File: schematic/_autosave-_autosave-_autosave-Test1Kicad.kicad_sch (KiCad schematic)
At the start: 49 parts, among them IC1 BMI055, J1 Power Module 1, J2 Power Module 2, J3 USB, J4 Telemetry 1, J5 Telemetry 2, J6 UART & I2C B, J7 CAN 1, J8 CAN 2, J9 GPS Module, U1 STM32F765IIKx, U10 TJA1051TK-3, U11 LT3080xDD, U2 NEO-M8N, U3 IST8310, U4 ICM-20602, U5 ICM-20689, U6 MS5611-01BA, U7 LT3080xDD, U8 STM32F103V8Tx, U9 TJA1051TK-3, Y1 ABM2-8.000MHZ-D4Y-T

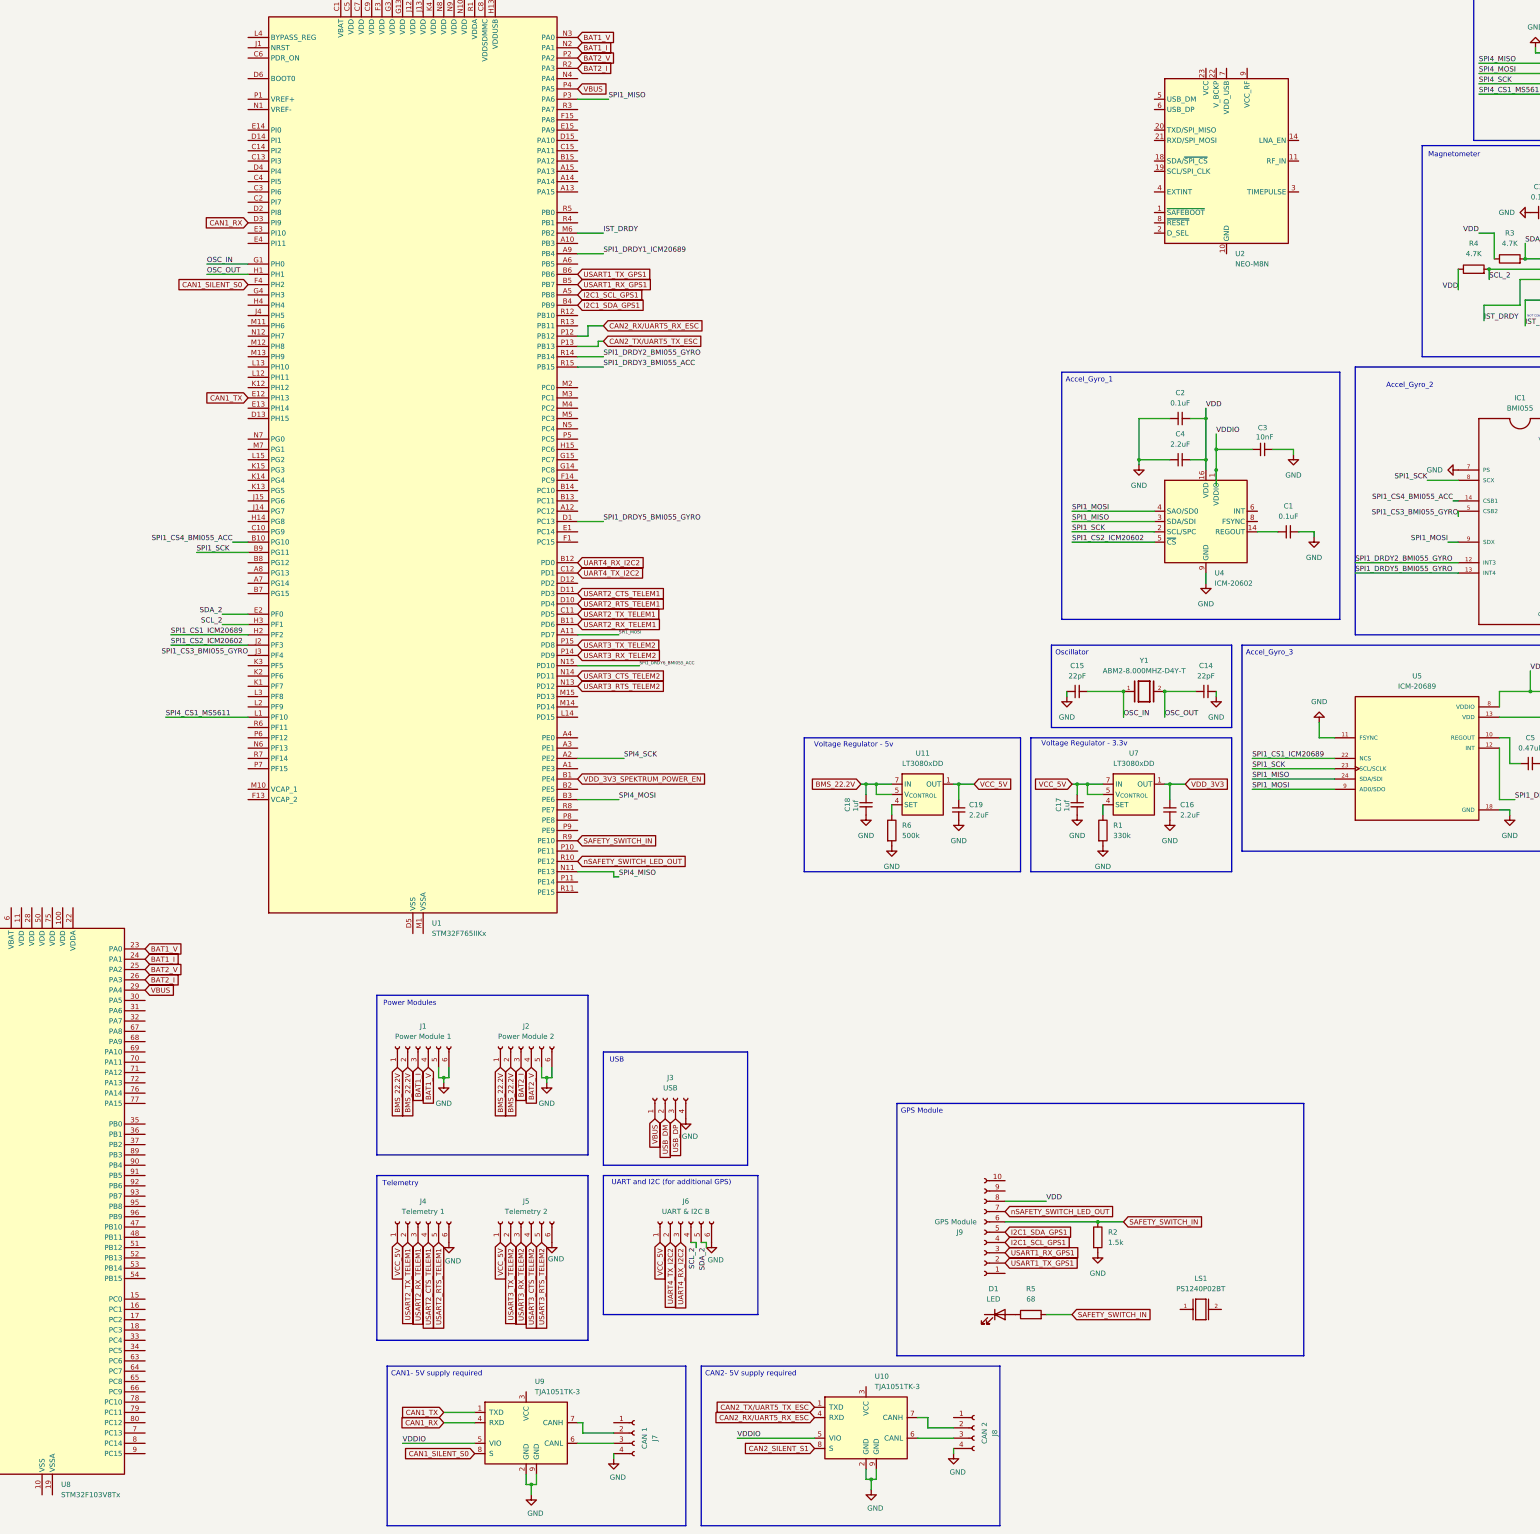
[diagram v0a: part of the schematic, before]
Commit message: CAP&ADC IN and SPI ports
also renamed UART&I2CB's SDA and SCL wire labels
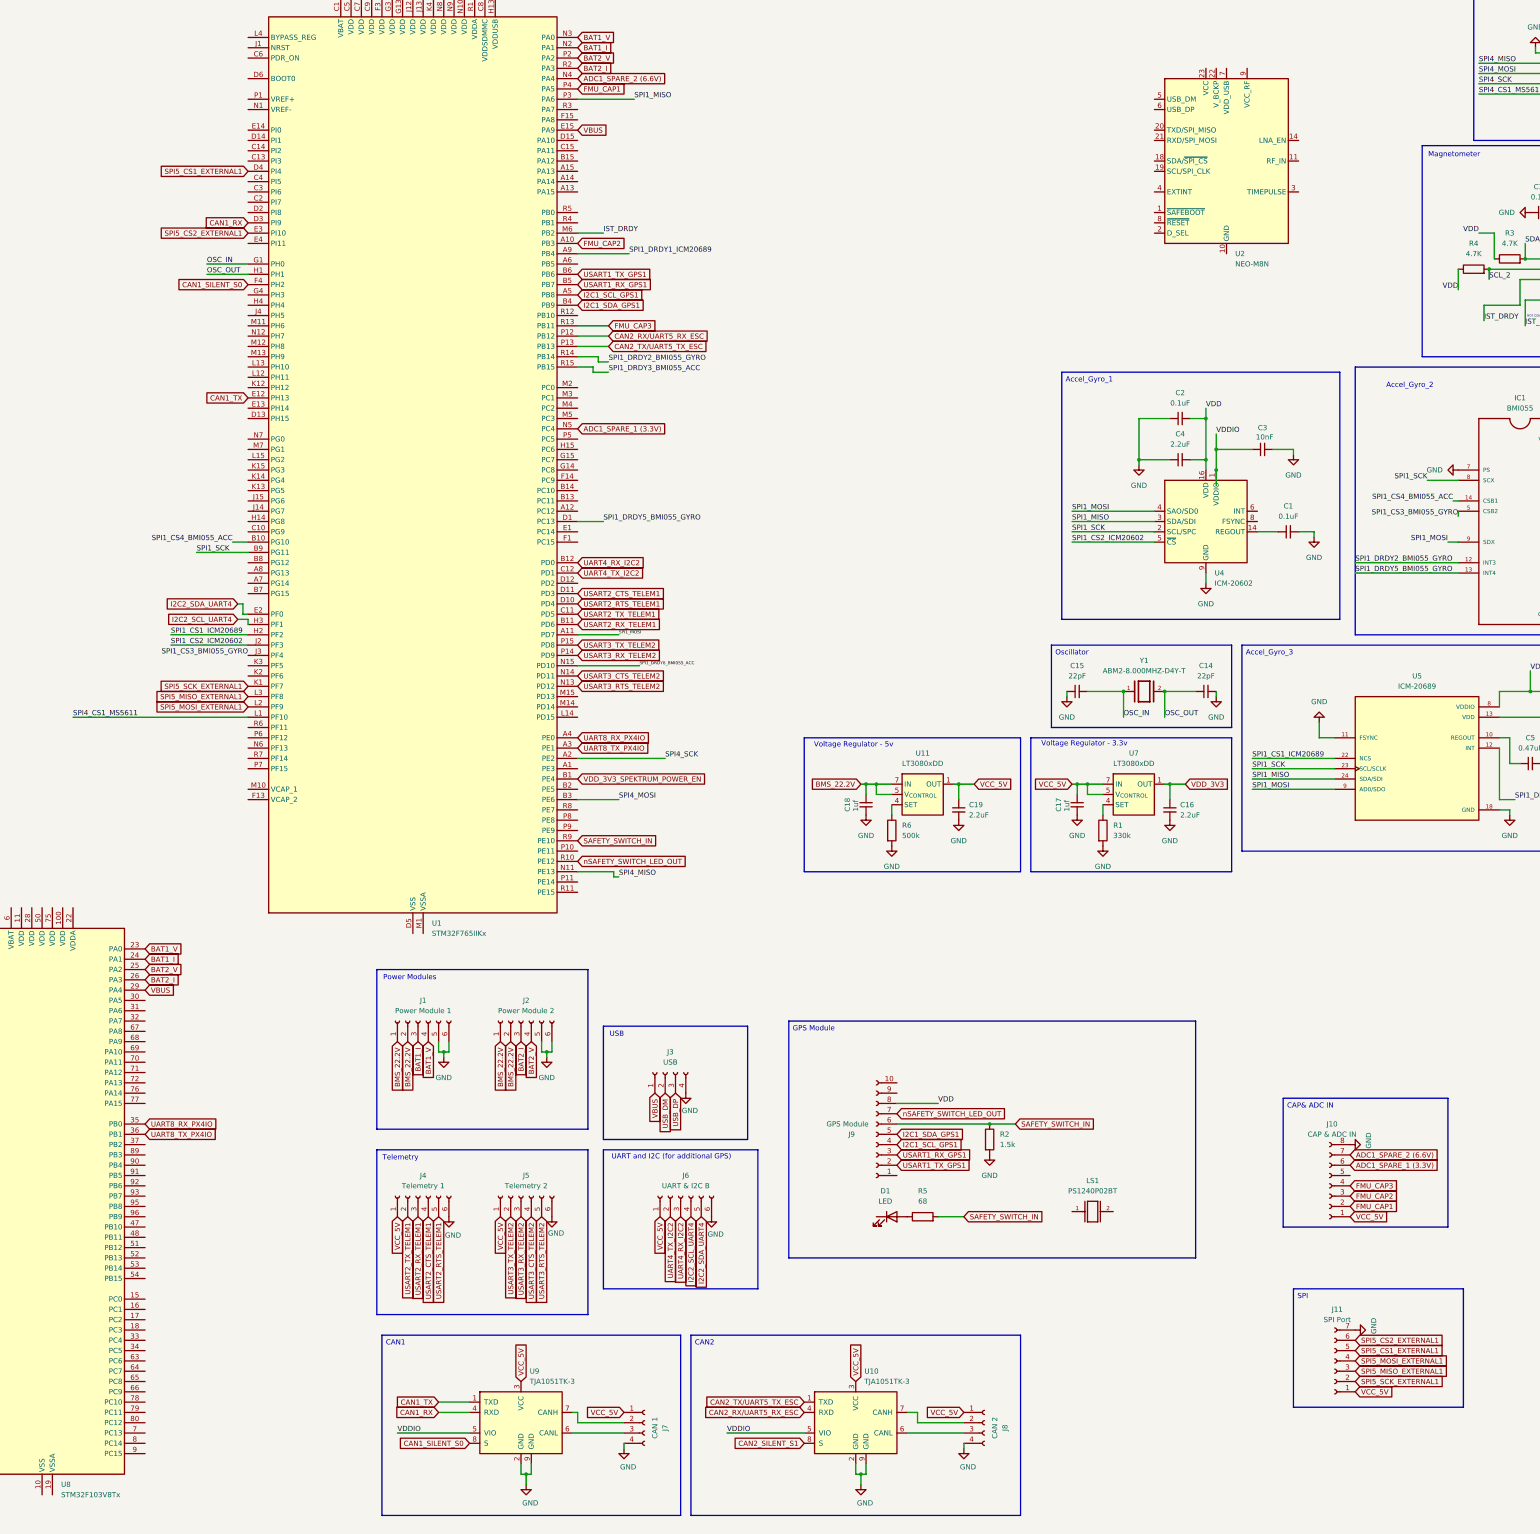
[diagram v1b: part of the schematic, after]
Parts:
- added J10: CAP & ADC IN, symbol Connector:Conn_01x08_Socket
- added J11: SPI Port, symbol Connector:Conn_01x07_Socket
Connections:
- net GND: now also J10.8 (Pin_8), J11.7 (Pin_7)
- net SCL_2: no longer J6.4 (Pin_4), U1.H3 (PF1)
- net SDA_2: no longer J6.5 (Pin_5), U1.E2 (PF0)
- net VBUS: now also U1.E15 (PA9); no longer U1.P4 (PA5)
- net VCC_5V: now also J7.1 (Pin_1), J8.1 (Pin_1), U10.3 (VCC), U9.3 (VCC), J10.1 (Pin_1), J11.1 (Pin_1)
- net FMU_CAP2: now reaches U1.A10 (PB3)
- net FMU_CAP2: now also J10.3 (Pin_3)
- net UART8_TX_PX4IO: now reaches U1.A3 (PE1)
- net UART8_TX_PX4IO: now also U8.36 (PB1)
- net UART8_RX_PX4IO: now reaches U1.A4 (PE0)
- net UART8_RX_PX4IO: now also U8.35 (PB0)
- net SPI5_CS1_EXTERNAL1: now reaches U1.D4 (PI4)
- net SPI5_CS1_EXTERNAL1: now also J11.5 (Pin_5)
- net SPI5_CS2_EXTERNAL1: now reaches U1.E3 (PI10)
- net SPI5_CS2_EXTERNAL1: now also J11.6 (Pin_6)
- net SPI5_SCK_EXTERNAL1: now reaches U1.K1 (PF7)
- net SPI5_SCK_EXTERNAL1: now also J11.2 (Pin_2)
- net SPI5_MOSI_EXTERNAL1: now reaches U1.L2 (PF9)
- net SPI5_MOSI_EXTERNAL1: now also J11.4 (Pin_4)
- net SPI5_MISO_EXTERNAL1: now reaches U1.L3 (PF8)
- net SPI5_MISO_EXTERNAL1: now also J11.3 (Pin_3)
- net ADC1_SPARE_2 (6.6V): now reaches U1.N4 (PA4)
- net ADC1_SPARE_2 (6.6V): now also J10.7 (Pin_7)
- net ADC1_SPARE_1 (3.3V): now reaches U1.N5 (PC4)
- net ADC1_SPARE_1 (3.3V): now also J10.6 (Pin_6)
- net FMU_CAP3: now reaches U1.R13 (PB11)
- net FMU_CAP3: now also J10.4 (Pin_4)
- new net FMU_CAP1: J10.2 (Pin_2), U1.P4 (PA5)
- new net I2C2_SCL_UART4: J6.4 (Pin_4), U1.H3 (PF1)
- new net I2C2_SDA_UART4: J6.5 (Pin_5), U1.E2 (PF0)
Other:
- moved on the sheet: D1, J1, J2, J3, J4, J5, J6, J7, J8, J9, LS1, R2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

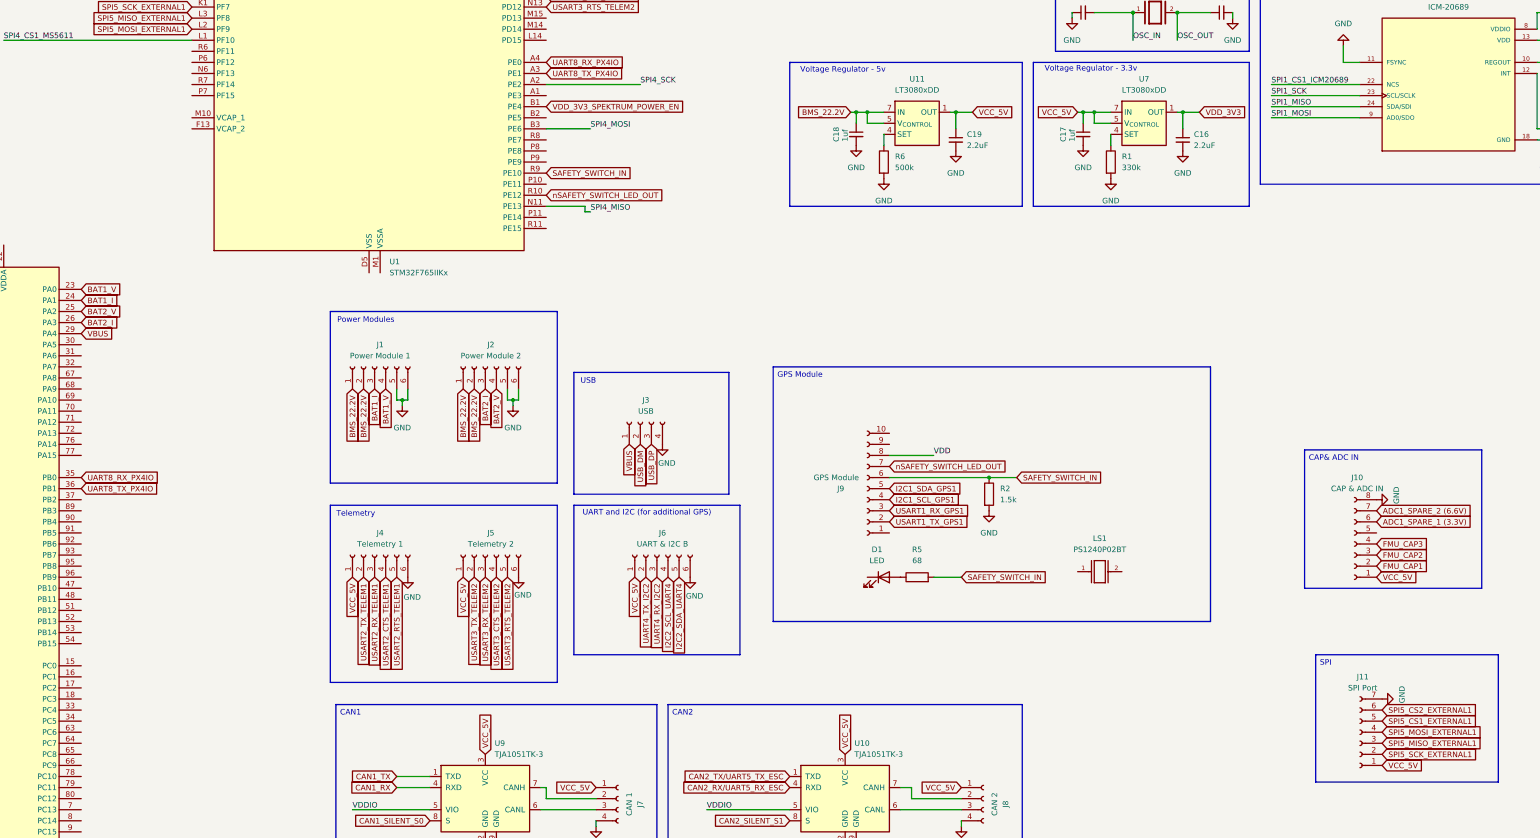
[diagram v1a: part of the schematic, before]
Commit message: I2C A port
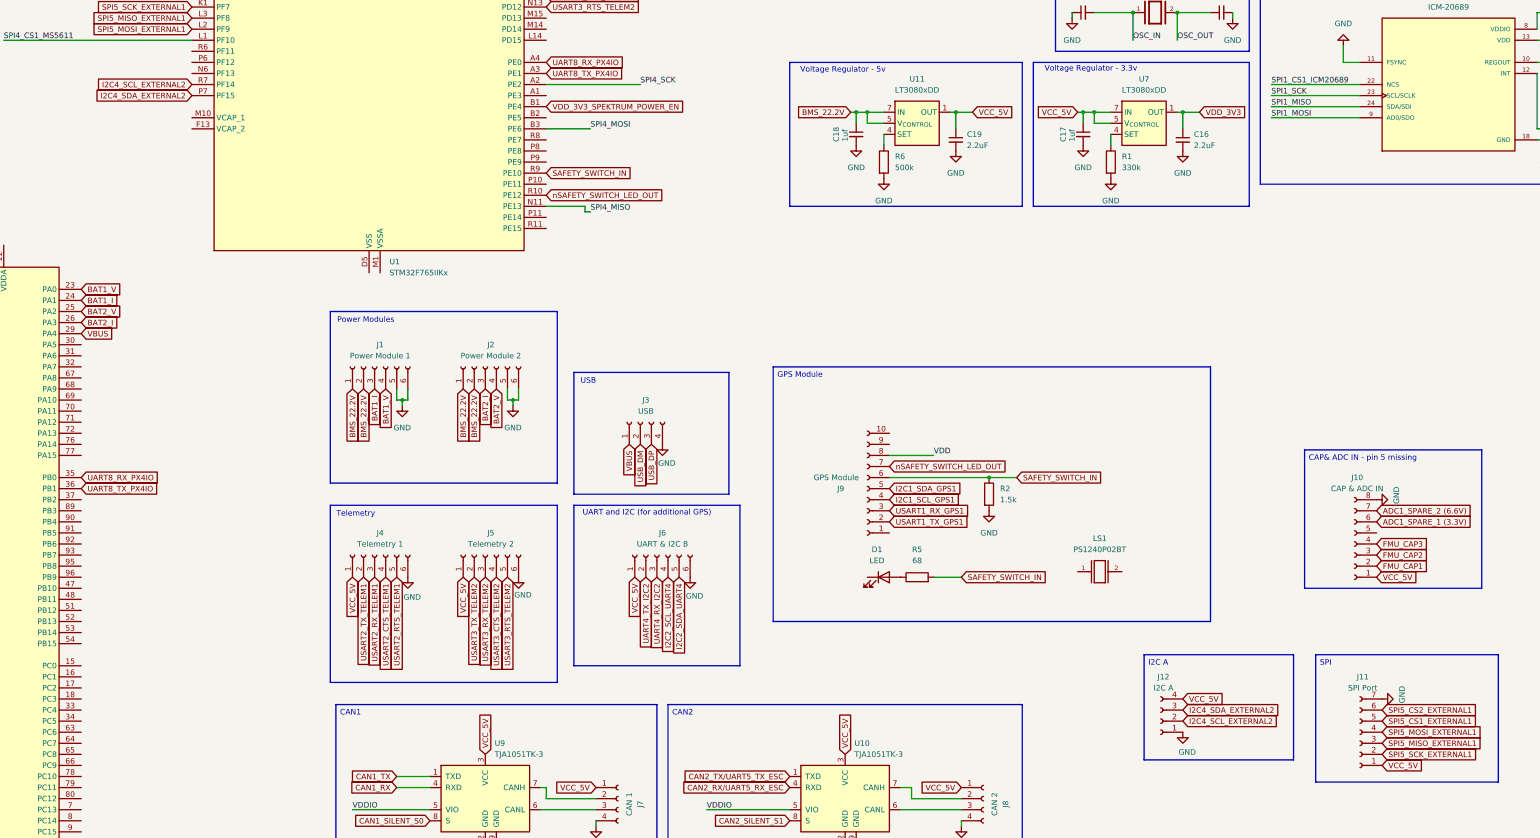
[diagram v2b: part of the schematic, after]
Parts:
- added J12: I2C A, symbol Connector:Conn_01x04_Socket
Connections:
- net GND: now also J12.1 (Pin_1)
- net VCC_5V: now also J12.4 (Pin_4)
- net I2C4_SDA_EXTERNAL2: now reaches U1.P7 (PF15)
- net I2C4_SDA_EXTERNAL2: now also J12.3 (Pin_3)
- net I2C4_SCL_EXTERNAL2: now reaches U1.R7 (PF14)
- net I2C4_SCL_EXTERNAL2: now also J12.2 (Pin_2)

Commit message: PPM RC port
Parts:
- added J13: FMU PWM OUT, symbol Connector:Conn_01x10_Socket
- added J14: PPM RC, symbol Connector:Conn_01x03_Socket
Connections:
- net GND: now also J13.10 (Pin_10), J14.3 (Pin_3)
- net VCC_5V: now also J14.1 (Pin_1)
- net RC_INPUT (aka PPM_IN): now reaches U1.C4 (PI5)
- net RC_INPUT (aka PPM_IN): now also J14.2 (Pin_2)
- net FMU_CH2: now reaches U1.D15 (PA10)
- net FMU_CH2: now also J13.3 (Pin_3)
- net FMU_CH7: now reaches U1.M11 (PH6)
- net FMU_CH7: now also J13.8 (Pin_8)
- net FMU_CH8: now reaches U1.M13 (PH9)
- net FMU_CH8: now also J13.9 (Pin_9)
- net FMU_CH6: now reaches U1.M14 (PD14)
- net FMU_CH6: now also J13.7 (Pin_7)
- net FMU_CH5: now reaches U1.M15 (PD13)
- net FMU_CH5: now also J13.6 (Pin_6)
- net FMU_CH3: now reaches U1.P10 (PE11)
- net FMU_CH3: now also J13.4 (Pin_4)
- net FMU_CH1: now reaches U1.P11 (PE14)
- net FMU_CH1: now also J13.2 (Pin_2)
- net FMU_CH4: now reaches U1.P9 (PE9)
- net FMU_CH4: now also J13.5 (Pin_5)
- no-connect marks 3 -> 4

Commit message: Added micro SD port, updated CAN
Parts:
- added C20, C25: 4.7nF, symbol Device:C_Small
- added C21, C22, C23, C24: 100pF, symbol Device:C_Small
- added C26, C27: 100nF, symbol Device:C_Small
- added J15: 2908-05WB-MG, 2908-05WB-MG:3M_2908-05WB-MG, symbol 2908-05WB-MG:2908-05WB-MG
- added R10, R11, R7, R8, R9: 100k, symbol Device:R
- added R12, R13, R14, R15: 60, symbol Device:R
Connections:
- net GND: now also C20.2, C21.1, C22.1, C23.1, C24.1, C25.2, J15.6 (VSS)
- net VCC_5V: now also C26.1, C27.1
- net VDDIO: now also C26.2, C27.2
- net SDMMC1_CLK: now reaches U1.A12 (PC12)
- net SDMMC1_CLK: now also J15.5 (CLK)
- net SDMMC1_D3: now reaches U1.B13 (PC11)
- net SDMMC1_D3: now also J15.2 (DAT3/CD), R7.1
- net SDMMC1_D2: now reaches U1.B14 (PC10)
- net SDMMC1_D2: now also J15.1 (DAT2), R9.1
- net SDMMC1_CMD: now reaches U1.D12 (PD2)
- net SDMMC1_CMD: now also J15.3 (CMD), R8.1
- net SDMMC1_D1: now reaches U1.F14 (PC9)
- net SDMMC1_D1: now also J15.8 (DAT1), R10.1
- net SDMMC1_D0: now reaches U1.G14 (PC8)
- net SDMMC1_D0: now also J15.7 (DAT0), R11.1
- net at J8.2 (Pin_2): now also J8.3 (Pin_3), C20.1, R12.2, R13.2; no longer U10.7 (CANH)
- net at U10.6 (CANL): now also C21.2, R13.1; no longer J8.3 (Pin_3)
- net at J7.2 (Pin_2): now also J7.3 (Pin_3), C25.1, R14.2, R15.2; no longer U9.7 (CANH)
- net at U9.6 (CANL): now also C23.2, R15.1; no longer J7.3 (Pin_3)
- new net: J15.4 (VDD), R10.2, R11.2, R7.2, R8.2, R9.2
- new net: C24.2, R14.1, U9.7 (CANH)
- new net: C22.2, R12.1, U10.7 (CANH)
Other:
- moved on the sheet: D1, J10, J11, J12, J13, J14, J7, J8, J9, LS1, R2, R5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
